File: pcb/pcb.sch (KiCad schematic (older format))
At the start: 37 parts, among them J1 Conn_01x10, J2 Conn_01x05, J3 Conn_01x05, J4 Conn_01x05, J5 Conn_01x05, J6 Conn_01x05, J7 Conn_01x05, J8 Conn_01x05, U1 teensy-2.0

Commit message: Final routing of base pcb. Outline left.
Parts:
- removed J8: Conn_01x05, keyboard-parts:header_1x05_2.54mm, symbol Connector_Generic:Conn_01x05
- J1: footprint keyboard-parts:header_1x10_1.27mm -> keyboard-parts:header_2x05_2.54mm
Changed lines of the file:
@@
 EESchema Schematic File Version 4
+LIBS:pcb-cache
 EELAYER 30 0
 EELAYER END
@@
 F 0 "J1" H 9450 2100 50  0000 C CNN
 F 1 "Conn_01x10" H 9450 1000 50  0000 C CNN
-F 2 "keyboard-parts:header_1x10_1.27mm" H 9450 1600 50  0001 C CNN
+F 2 "keyboard-parts:header_2x05_2.54mm" H 9450 1600 50  0001 C CNN
 F 3 "~" H 9450 1600 50  0001 C CNN
 	1    9450 1600
@@
 	1    0    0    -1
 $EndComp
-$Comp
-L Connector_Generic:Conn_01x05 J8
-U 1 1 5EF89583
-P 10725 6050
-F 0 "J8" H 10725 6350 50  0000 C CNN
-F 1 "Conn_01x05" H 10725 5750 50  0000 C CNN
-F 2 "keyboard-parts:header_1x05_2.54mm" H 10725 6050 50  0001 C CNN
-F 3 "~" H 10725 6050 50  0001 C CNN
-	1    10725 6050
-	1    0    0    -1
-$EndComp
 Wire Wire Line
 	7525 5850 7525 5950
@@
 Wire Wire Line
 	10025 6150 10025 6250
-Wire Wire Line
-	10525 5850 10525 5950
-Connection ~ 10525 5950
-Wire Wire Line
-	10525 5950 10525 6050
-Connection ~ 10525 6050
-Wire Wire Line
-	10525 6050 10525 6150
-Connection ~ 10525 6150
-Wire Wire Line
-	10525 6150 10525 6250
 Text Label 1175 3425 2    50   ~ 0
 Ext-C0-CB

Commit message: Add headers for board interconnect
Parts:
- removed JP1, JP2, JP3, JP4, JP5, JP6: SolderJumper_2_Open, keyboard-parts:solder-jumper-2p-open, symbol Jumper:SolderJumper_2_Open
- added J8: Conn_01x10, keyboard-parts:idc-header_2x05_2.54mm, symbol Connector_Generic:Conn_01x10
- J1: footprint keyboard-parts:header_2x05_2.54mm -> keyboard-parts:idc-header_2x05_2.54mm
- U1: footprint keyboard-parts:teensy2.0 -> keyboard-parts:teensy2.0_dualside
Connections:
- net C0-CB: now also J8.10 (Pin_10)
- net C1-CA: now also J8.9 (Pin_9)
- net C2-C9: now also J8.8 (Pin_8)
- net C3-C8: now also J8.7 (Pin_7)
- net C4-C7: now also J8.6 (Pin_6)
- net C5-C6: now also J8.5 (Pin_5)
- net R0: now also J8.1 (Pin_1)
- net R1: now also J8.2 (Pin_2)
- net R2: now also J8.3 (Pin_3)
- net R3: now also J8.4 (Pin_4)
- net Ext-C0-CB: no longer names the net of J1.10 (Pin_10), U1.18 (PD6_ADC9_T1_OC4D_LED)
- net Ext-C1-CA: no longer names the net of J1.9 (Pin_9), U1.19 (PD7_ADC10_T0_OC4D)
- net Ext-C2-C9: no longer names the net of J1.8 (Pin_8), U1.20 (PB4_ADC11)
- net Ext-C3-C8: no longer names the net of J1.7 (Pin_7), U1.21 (PB5_ADC12_OC1A_OB4B)
- net Ext-C4-C7: no longer names the net of J1.6 (Pin_6), U1.22 (PB6_ADC13_OC1B_OC4B)
- net Ext-C5-C6: no longer names the net of J1.5 (Pin_5), U1.23 (PF7_ADC7)
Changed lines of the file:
@@
 F 0 "U1" H 6550 2700 60  0000 C CNN
 F 1 "teensy-2.0" H 8250 600 60  0000 C CNN
-F 2 "keyboard-parts:teensy2.0" H 7600 700 60  0001 C CNN
+F 2 "keyboard-parts:teensy2.0_dualside" H 7600 700 60  0001 C CNN
 F 3 "" H 7600 700 60  0001 C CNN
 	1    7500 1750
@@
 Text Label 6300 2100 2    50   ~ 0
 C0-CB
-Text Label 8700 1600 0    50   ~ 0
-Ext-C5-C6
-Text Label 8700 1700 0    50   ~ 0
-Ext-C4-C7
-Text Label 8700 1800 0    50   ~ 0
-Ext-C3-C8
-Text Label 8700 1900 0    50   ~ 0
-Ext-C2-C9
-Text Label 8700 2000 0    50   ~ 0
-Ext-C1-CA
-Text Label 8700 2100 0    50   ~ 0
-Ext-C0-CB
 NoConn ~ 8700 1300
 NoConn ~ 8700 1200
@@
 F 0 "J1" H 9450 2100 50  0000 C CNN
 F 1 "Conn_01x10" H 9450 1000 50  0000 C CNN
-F 2 "keyboard-parts:header_2x05_2.54mm" H 9450 1600 50  0001 C CNN
+F 2 "keyboard-parts:idc-header_2x05_2.54mm" H 9450 1600 50  0001 C CNN
 F 3 "~" H 9450 1600 50  0001 C CNN
 	1    9450 1600
@@
 Wire Wire Line
 	10025 6150 10025 6250
-Text Label 1175 3425 2    50   ~ 0
-Ext-C0-CB
-Text Label 1925 3425 2    50   ~ 0
-Ext-C1-CA
-Text Label 2675 3425 2    50   ~ 0
-Ext-C2-C9
-Text Label 3425 3425 2    50   ~ 0
-Ext-C3-C8
-Text Label 4175 3425 2    50   ~ 0
-Ext-C4-C7
-Text Label 4925 3425 2    50   ~ 0
-Ext-C5-C6
 Wire Wire Line
 	1175 2000 1175 2500
 Connection ~ 1175 2500
 Wire Wire Line
-	1175 2500 1175 3125
-Wire Wire Line
 	1925 1500 1925 2000
 Connection ~ 1925 2000
 Wire Wire Line
-	1925 2000 1925 3125
-Wire Wire Line
 	2675 1500 2675 2000
 Connection ~ 2675 2000
 Wire Wire Line
-	2675 2000 2675 3125
-Wire Wire Line
 	3425 2000 3425 2500
 Connection ~ 3425 2500
 Wire Wire Line
-	3425 2500 3425 3125
-Wire Wire Line
 	4175 2000 4175 2500
 Connection ~ 4175 2500
 Wire Wire Line
-	4175 2500 4175 3125
-Wire Wire Line
 	4925 2000 4925 2500
 Connection ~ 4925 2500
-Wire Wire Line
-	4925 2500 4925 3125
-$Comp
-L Jumper:SolderJumper_2_Open JP1
-U 1 1 5EFDA2A9
-P 1175 3275
-F 0 "JP1" H 1175 3355 50  0000 C CNN
-F 1 "SolderJumper_2_Open" H 1175 3175 50  0000 C CNN
-F 2 "keyboard-parts:solder-jumper-2p-open" H 1175 3275 50  0001 C CNN
-F 3 "~" H 1175 3275 50  0001 C CNN
-	1    1175 3275
-	0    1    1    0
-$EndComp
-$Comp
-L Jumper:SolderJumper_2_Open JP2
-U 1 1 5EFDBA8A
-P 1925 3275
-F 0 "JP2" H 1925 3355 50  0000 C CNN
-F 1 "SolderJumper_2_Open" H 1925 3175 50  0000 C CNN
-F 2 "keyboard-parts:solder-jumper-2p-open" H 1925 3275 50  0001 C CNN
-F 3 "~" H 1925 3275 50  0001 C CNN
-	1    1925 3275
-	0    1    1    0
-$EndComp
-$Comp
-L Jumper:SolderJumper_2_Open JP3
-U 1 1 5EFDC256
-P 2675 3275
-F 0 "JP3" H 2675 3355 50  0000 C CNN
-F 1 "SolderJumper_2_Open" H 2675 3175 50  0000 C CNN
-F 2 "keyboard-parts:solder-jumper-2p-open" H 2675 3275 50  0001 C CNN
-F 3 "~" H 2675 3275 50  0001 C CNN
-	1    2675 3275
-	0    1    1    0
-$EndComp
-$Comp
-L Jumper:SolderJumper_2_Open JP4
-U 1 1 5EFDC8C1
-P 3425 3275
-F 0 "JP4" H 3425 3355 50  0000 C CNN
-F 1 "SolderJumper_2_Open" H 3425 3175 50  0000 C CNN
-F 2 "keyboard-parts:solder-jumper-2p-open" H 3425 3275 50  0001 C CNN
-F 3 "~" H 3425 3275 50  0001 C CNN
-	1    3425 3275
-	0    1    1    0
-$EndComp
-$Comp
-L Jumper:SolderJumper_2_Open JP5
-U 1 1 5EFDCEED
-P 4175 3275
-F 0 "JP5" H 4175 3355 50  0000 C CNN
-F 1 "SolderJumper_2_Open" H 4175 3175 50  0000 C CNN
-F 2 "keyboard-parts:solder-jumper-2p-open" H 4175 3275 50  0001 C CNN
-F 3 "~" H 4175 3275 50  0001 C CNN
-	1    4175 3275
-	0    1    1    0
-$EndComp
-$Comp
-L Jumper:SolderJumper_2_Open JP6
-U 1 1 5EFDD2B4
-P 4925 3275
-F 0 "JP6" H 4925 3355 50  0000 C CNN
-F 1 "SolderJumper_2_Open" H 4925 3175 50  0000 C CNN
-F 2 "keyboard-parts:solder-jumper-2p-open" H 4925 3275 50  0001 C CNN
-F 3 "~" H 4925 3275 50  0001 C CNN
-	1    4925 3275
-	0    1    1    0
-$EndComp
+$Comp
+L Connector_Generic:Conn_01x10 J8
+U 1 1 5EF5D373
+P 5900 3325
+F 0 "J8" H 5900 3825 50  0000 C CNN
+F 1 "Conn_01x10" H 5900 2725 50  0000 C CNN
+F 2 "keyboard-parts:idc-header_2x05_2.54mm" H 5900 3325 50  0001 C CNN
+F 3 "~" H 5900 3325 50  0001 C CNN
+	1    5900 3325
+	1    0    0    -1
+$EndComp
+Text Label 5700 2925 2    50   ~ 0
+R0
+Text Label 5700 3025 2    50   ~ 0
+R1
+Text Label 5700 3125 2    50   ~ 0
+R2
+Text Label 5700 3225 2    50   ~ 0
+R3
+Wire Wire Line
+	4925 2500 4925 3325
+Wire Wire Line
+	4175 2500 4175 3425
+Wire Wire Line
+	3425 2500 3425 3525
+Wire Wire Line
+	2675 2000 2675 3625
+Wire Wire Line
+	1925 2000 1925 3725
+Wire Wire Line
+	1175 2500 1175 3825
+Wire Wire Line
+	4925 3325 5700 3325
+Wire Wire Line
+	3425 3525 5700 3525
+Wire Wire Line
+	2675 3625 5700 3625
+Wire Wire Line
+	1925 3725 5700 3725
+Wire Wire Line
+	1175 3825 5700 3825
+Wire Wire Line
+	4175 3425 5700 3425
 $EndSCHEMATC

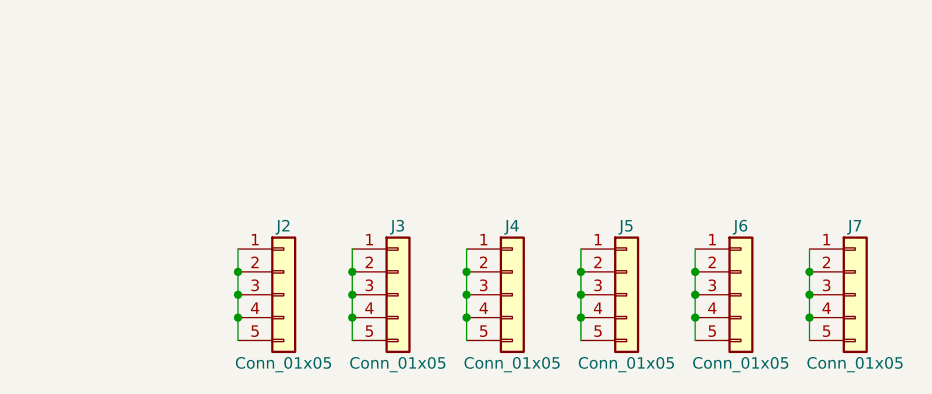
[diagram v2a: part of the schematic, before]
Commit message: Update board outline
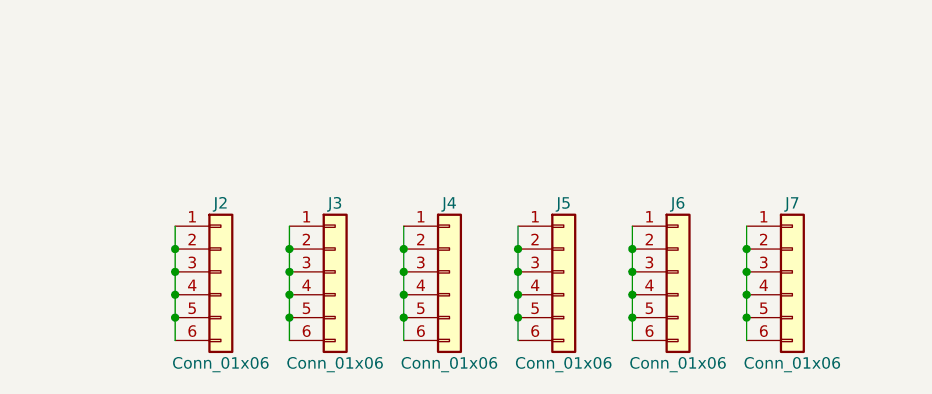
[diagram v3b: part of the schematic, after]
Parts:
- removed J2, J3, J4, J5, J6, J7: Conn_01x05, keyboard-parts:header_1x05_2.54mm, symbol Connector_Generic:Conn_01x05
- added J2, J3, J4, J5, J6, J7: Conn_01x06, keyboard-parts:header_1x06_2.54mm, symbol Connector_Generic:Conn_01x06
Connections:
- new net: J2.1 (Pin_1), J2.2 (Pin_2), J2.3 (Pin_3), J2.4 (Pin_4), J2.5 (Pin_5), J2.6 (Pin_6)
- new net: J3.1 (Pin_1), J3.2 (Pin_2), J3.3 (Pin_3), J3.4 (Pin_4), J3.5 (Pin_5), J3.6 (Pin_6)
- new net: J4.1 (Pin_1), J4.2 (Pin_2), J4.3 (Pin_3), J4.4 (Pin_4), J4.5 (Pin_5), J4.6 (Pin_6)
- new net: J5.1 (Pin_1), J5.2 (Pin_2), J5.3 (Pin_3), J5.4 (Pin_4), J5.5 (Pin_5), J5.6 (Pin_6)
- new net: J6.1 (Pin_1), J6.2 (Pin_2), J6.3 (Pin_3), J6.4 (Pin_4), J6.5 (Pin_5), J6.6 (Pin_6)
- new net: J7.1 (Pin_1), J7.2 (Pin_2), J7.3 (Pin_3), J7.4 (Pin_4), J7.5 (Pin_5), J7.6 (Pin_6)
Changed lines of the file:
@@
 Text Label 9250 1500 2    50   ~ 0
 R3
-$Comp
-L Connector_Generic:Conn_01x05 J2
-U 1 1 5EF80B00
-P 7725 6050
-F 0 "J2" H 7725 6350 50  0000 C CNN
-F 1 "Conn_01x05" H 7725 5750 50  0000 C CNN
-F 2 "keyboard-parts:header_1x05_2.54mm" H 7725 6050 50  0001 C CNN
-F 3 "~" H 7725 6050 50  0001 C CNN
-	1    7725 6050
-	1    0    0    -1
-$EndComp
-$Comp
-L Connector_Generic:Conn_01x05 J3
-U 1 1 5EF87223
-P 8225 6050
-F 0 "J3" H 8225 6350 50  0000 C CNN
-F 1 "Conn_01x05" H 8225 5750 50  0000 C CNN
-F 2 "keyboard-parts:header_1x05_2.54mm" H 8225 6050 50  0001 C CNN
-F 3 "~" H 8225 6050 50  0001 C CNN
-	1    8225 6050
-	1    0    0    -1
-$EndComp
-$Comp
-L Connector_Generic:Conn_01x05 J4
-U 1 1 5EF87CB1
-P 8725 6050
-F 0 "J4" H 8725 6350 50  0000 C CNN
-F 1 "Conn_01x05" H 8725 5750 50  0000 C CNN
-F 2 "keyboard-parts:header_1x05_2.54mm" H 8725 6050 50  0001 C CNN
-F 3 "~" H 8725 6050 50  0001 C CNN
-	1    8725 6050
-	1    0    0    -1
-$EndComp
-$Comp
-L Connector_Generic:Conn_01x05 J5
-U 1 1 5EF881B8
-P 9225 6050
-F 0 "J5" H 9225 6350 50  0000 C CNN
-F 1 "Conn_01x05" H 9225 5750 50  0000 C CNN
-F 2 "keyboard-parts:header_1x05_2.54mm" H 9225 6050 50  0001 C CNN
-F 3 "~" H 9225 6050 50  0001 C CNN
-	1    9225 6050
-	1    0    0    -1
-$EndComp
-$Comp
-L Connector_Generic:Conn_01x05 J6
-U 1 1 5EF8886B
-P 9725 6050
-F 0 "J6" H 9725 6350 50  0000 C CNN
-F 1 "Conn_01x05" H 9725 5750 50  0000 C CNN
-F 2 "keyboard-parts:header_1x05_2.54mm" H 9725 6050 50  0001 C CNN
-F 3 "~" H 9725 6050 50  0001 C CNN
-	1    9725 6050
-	1    0    0    -1
-$EndComp
-$Comp
-L Connector_Generic:Conn_01x05 J7
-U 1 1 5EF890D6
-P 10225 6050
-F 0 "J7" H 10225 6350 50  0000 C CNN
-F 1 "Conn_01x05" H 10225 5750 50  0000 C CNN
-F 2 "keyboard-parts:header_1x05_2.54mm" H 10225 6050 50  0001 C CNN
-F 3 "~" H 10225 6050 50  0001 C CNN
-	1    10225 6050
-	1    0    0    -1
-$EndComp
-Wire Wire Line
-	7525 5850 7525 5950
-Connection ~ 7525 5950
-Wire Wire Line
-	7525 5950 7525 6050
-Connection ~ 7525 6050
-Wire Wire Line
-	7525 6050 7525 6150
-Connection ~ 7525 6150
-Wire Wire Line
-	7525 6150 7525 6250
-Wire Wire Line
-	8025 5850 8025 5950
-Connection ~ 8025 5950
-Wire Wire Line
-	8025 5950 8025 6050
-Connection ~ 8025 6050
-Wire Wire Line
-	8025 6050 8025 6150
-Connection ~ 8025 6150
-Wire Wire Line
-	8025 6150 8025 6250
-Wire Wire Line
-	8525 5850 8525 5950
-Connection ~ 8525 5950
-Wire Wire Line
-	8525 5950 8525 6050
-Connection ~ 8525 6050
-Wire Wire Line
-	8525 6050 8525 6150
-Connection ~ 8525 6150
-Wire Wire Line
-	8525 6150 8525 6250
-Wire Wire Line
-	9025 5850 9025 5950
-Connection ~ 9025 5950
-Wire Wire Line
-	9025 5950 9025 6050
-Connection ~ 9025 6050
-Wire Wire Line
-	9025 6050 9025 6150
-Connection ~ 9025 6150
-Wire Wire Line
-	9025 6150 9025 6250
-Wire Wire Line
-	9525 5850 9525 5950
-Connection ~ 9525 5950
-Wire Wire Line
-	9525 5950 9525 6050
-Connection ~ 9525 6050
-Wire Wire Line
-	9525 6050 9525 6150
-Connection ~ 9525 6150
-Wire Wire Line
-	9525 6150 9525 6250
-Wire Wire Line
-	10025 5850 10025 5950
-Connection ~ 10025 5950
-Wire Wire Line
-	10025 5950 10025 6050
-Connection ~ 10025 6050
-Wire Wire Line
-	10025 6050 10025 6150
-Connection ~ 10025 6150
-Wire Wire Line
-	10025 6150 10025 6250
 Wire Wire Line
 	1175 2000 1175 2500
@@
 Wire Wire Line
 	4175 3425 5700 3425
+$Comp
+L Connector_Generic:Conn_01x06 J2
+U 1 1 5EF6DF15
+P 7450 5950
+F 0 "J2" H 7450 6250 50  0000 C CNN
+F 1 "Conn_01x06" H 7450 5550 50  0000 C CNN
+F 2 "keyboard-parts:header_1x06_2.54mm" H 7450 5950 50  0001 C CNN
+F 3 "~" H 7450 5950 50  0001 C CNN
+	1    7450 5950
+	1    0    0    -1
+$EndComp
+$Comp
+L Connector_Generic:Conn_01x06 J3
+U 1 1 5EF726F1
+P 7950 5950
+F 0 "J3" H 7950 6250 50  0000 C CNN
+F 1 "Conn_01x06" H 7950 5550 50  0000 C CNN
+F 2 "keyboard-parts:header_1x06_2.54mm" H 7950 5950 50  0001 C CNN
+F 3 "~" H 7950 5950 50  0001 C CNN
+	1    7950 5950
+	1    0    0    -1
+$EndComp
+$Comp
+L Connector_Generic:Conn_01x06 J4
+U 1 1 5EF72FD2
+P 8450 5950
+F 0 "J4" H 8450 6250 50  0000 C CNN
+F 1 "Conn_01x06" H 8450 5550 50  0000 C CNN
+F 2 "keyboard-parts:header_1x06_2.54mm" H 8450 5950 50  0001 C CNN
+F 3 "~" H 8450 5950 50  0001 C CNN
+	1    8450 5950
+	1    0    0    -1
+$EndComp
+$Comp
+L Connector_Generic:Conn_01x06 J5
+U 1 1 5EF735AD
+P 8950 5950
+F 0 "J5" H 8950 6250 50  0000 C CNN
+F 1 "Conn_01x06" H 8950 5550 50  0000 C CNN
+F 2 "keyboard-parts:header_1x06_2.54mm" H 8950 5950 50  0001 C CNN
+F 3 "~" H 8950 5950 50  0001 C CNN
+	1    8950 5950
+	1    0    0    -1
+$EndComp
+$Comp
+L Connector_Generic:Conn_01x06 J6
+U 1 1 5EF73CAF
+P 9450 5950
+F 0 "J6" H 9450 6250 50  0000 C CNN
+F 1 "Conn_01x06" H 9450 5550 50  0000 C CNN
+F 2 "keyboard-parts:header_1x06_2.54mm" H 9450 5950 50  0001 C CNN
+F 3 "~" H 9450 5950 50  0001 C CNN
+	1    9450 5950
+	1    0    0    -1
+$EndComp
+$Comp
+L Connector_Generic:Conn_01x06 J7
+U 1 1 5EF744AF
+P 9950 5950
+F 0 "J7" H 9950 6250 50  0000 C CNN
+F 1 "Conn_01x06" H 9950 5550 50  0000 C CNN
+F 2 "keyboard-parts:header_1x06_2.54mm" H 9950 5950 50  0001 C CNN
+F 3 "~" H 9950 5950 50  0001 C CNN
+	1    9950 5950
+	1    0    0    -1
+$EndComp
+Wire Wire Line
+	7250 5750 7250 5850
+Connection ~ 7250 5850
+Wire Wire Line
+	7250 5850 7250 5950
+Connection ~ 7250 5950
+Wire Wire Line
+	7250 5950 7250 6050
+Connection ~ 7250 6050
+Wire Wire Line
+	7250 6050 7250 6150
+Connection ~ 7250 6150
+Wire Wire Line
+	7250 6150 7250 6250
+Wire Wire Line
+	7750 5750 7750 5850
+Connection ~ 7750 5850
+Wire Wire Line
+	7750 5850 7750 5950
+Connection ~ 7750 5950
+Wire Wire Line
+	7750 5950 7750 6050
+Connection ~ 7750 6050
+Wire Wire Line
+	7750 6050 7750 6150
+Connection ~ 7750 6150
+Wire Wire Line
+	7750 6150 7750 6250
+Wire Wire Line
+	8250 5750 8250 5850
+Connection ~ 8250 5850
+Wire Wire Line
+	8250 5850 8250 5950
+Connection ~ 8250 5950
+Wire Wire Line
+	8250 5950 8250 6050
+Connection ~ 8250 6050
+Wire Wire Line
+	8250 6050 8250 6150
+Connection ~ 8250 6150
+Wire Wire Line
+	8250 6150 8250 6250
+Wire Wire Line
+	8750 5750 8750 5850
+Connection ~ 8750 5850
+Wire Wire Line
+	8750 5850 8750 5950
+Connection ~ 8750 5950
+Wire Wire Line
+	8750 5950 8750 6050
+Connection ~ 8750 6050
+Wire Wire Line
+	8750 6050 8750 6150
+Connection ~ 8750 6150
+Wire Wire Line
+	8750 6150 8750 6250
+Wire Wire Line
+	9250 5750 9250 5850
+Connection ~ 9250 5850
+Wire Wire Line
+	9250 5850 9250 5950
+Connection ~ 9250 5950
+Wire Wire Line
+	9250 5950 9250 6050
+Connection ~ 9250 6050
+Wire Wire Line
+	9250 6050 9250 6150
+Connection ~ 9250 6150
+Wire Wire Line
+	9250 6150 9250 6250
+Wire Wire Line
+	9750 5750 9750 5850
+Connection ~ 9750 5850
+Wire Wire Line
+	9750 5850 9750 5950
+Connection ~ 9750 5950
+Wire Wire Line
+	9750 5950 9750 6050
+Connection ~ 9750 6050
+Wire Wire Line
+	9750 6050 9750 6150
+Connection ~ 9750 6150
+Wire Wire Line
+	9750 6150 9750 6250
 $EndSCHEMATC
